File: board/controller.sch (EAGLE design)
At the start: 33 parts, among them J1 X_SIG, J10 COOLANT, J12 VIN, J13 GND, J15 A_SIG, J16 +5V, J17 PROBE, J18 FEED_OVERRIDE, J19 MOTOR_CURRENT, J2 Y_SIG, J20 WHEEL, J21 IR_RECEIVER, J22 DISPLAY, J23 ERROR, J24 HOLDING, J25 SPINDLE, J26 SD_READER, J3 Z_SIG, J4 RESET, J5 Z_DISPLAY, J6 FEED_HOLD, J8 CYCLE_START

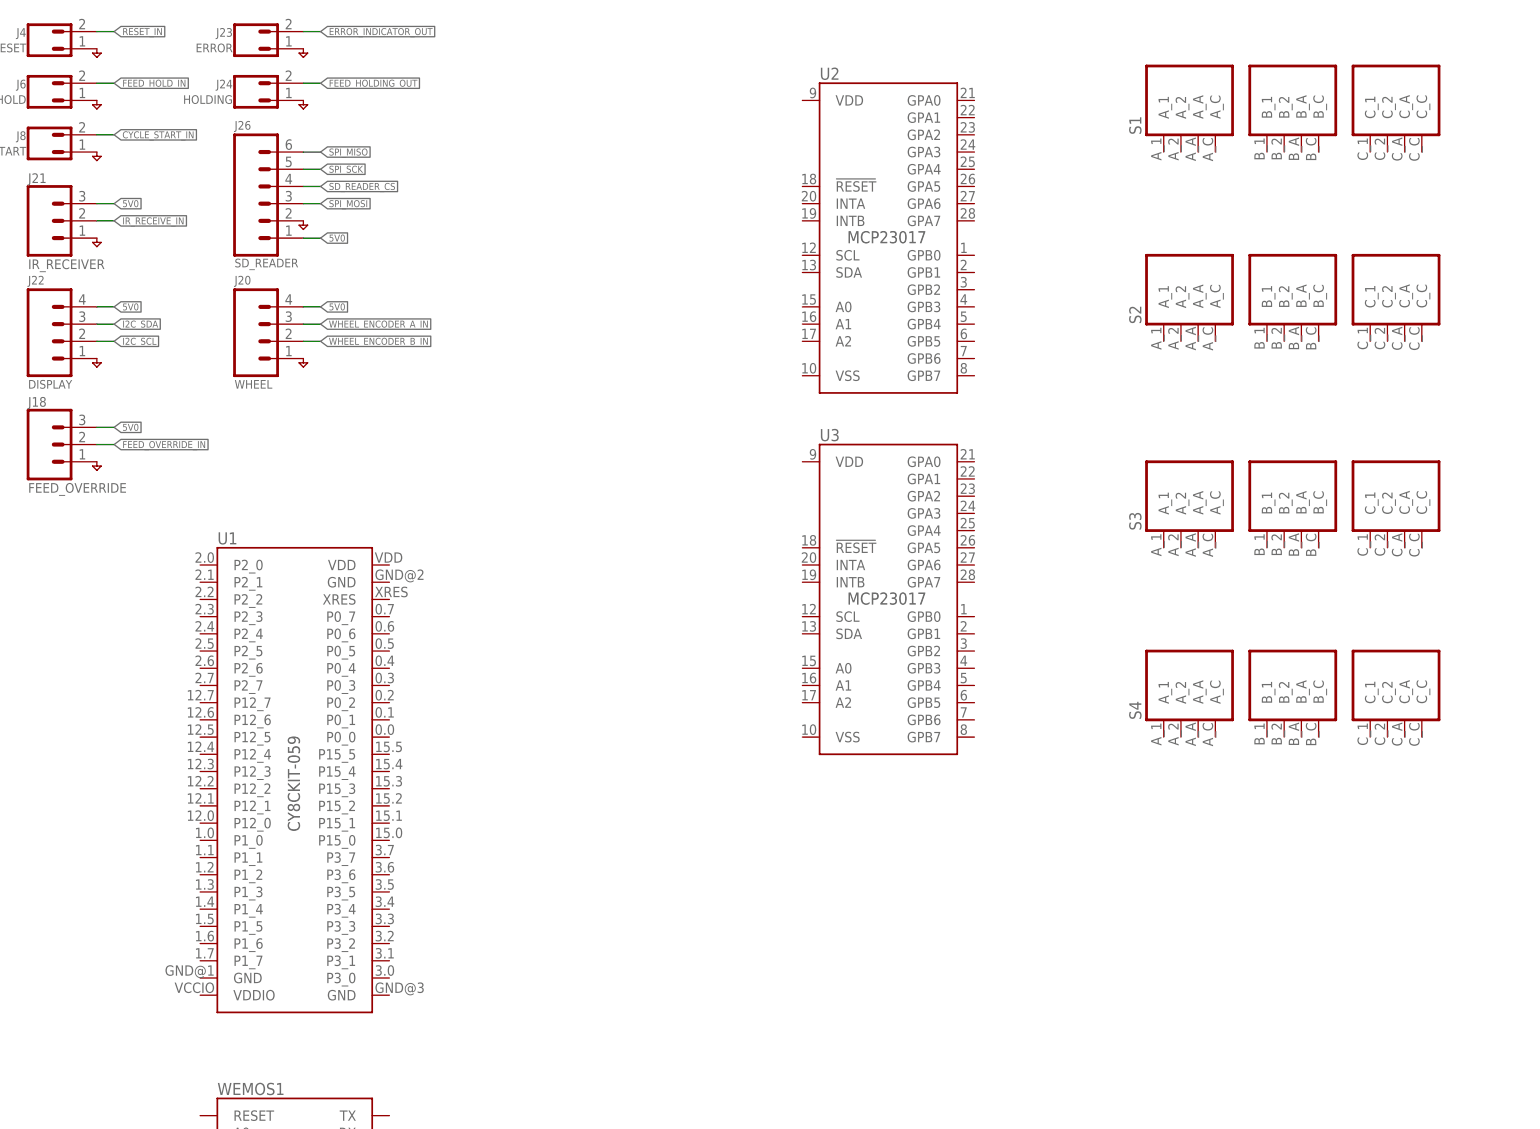
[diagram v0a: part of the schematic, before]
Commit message: started routing added datasheets
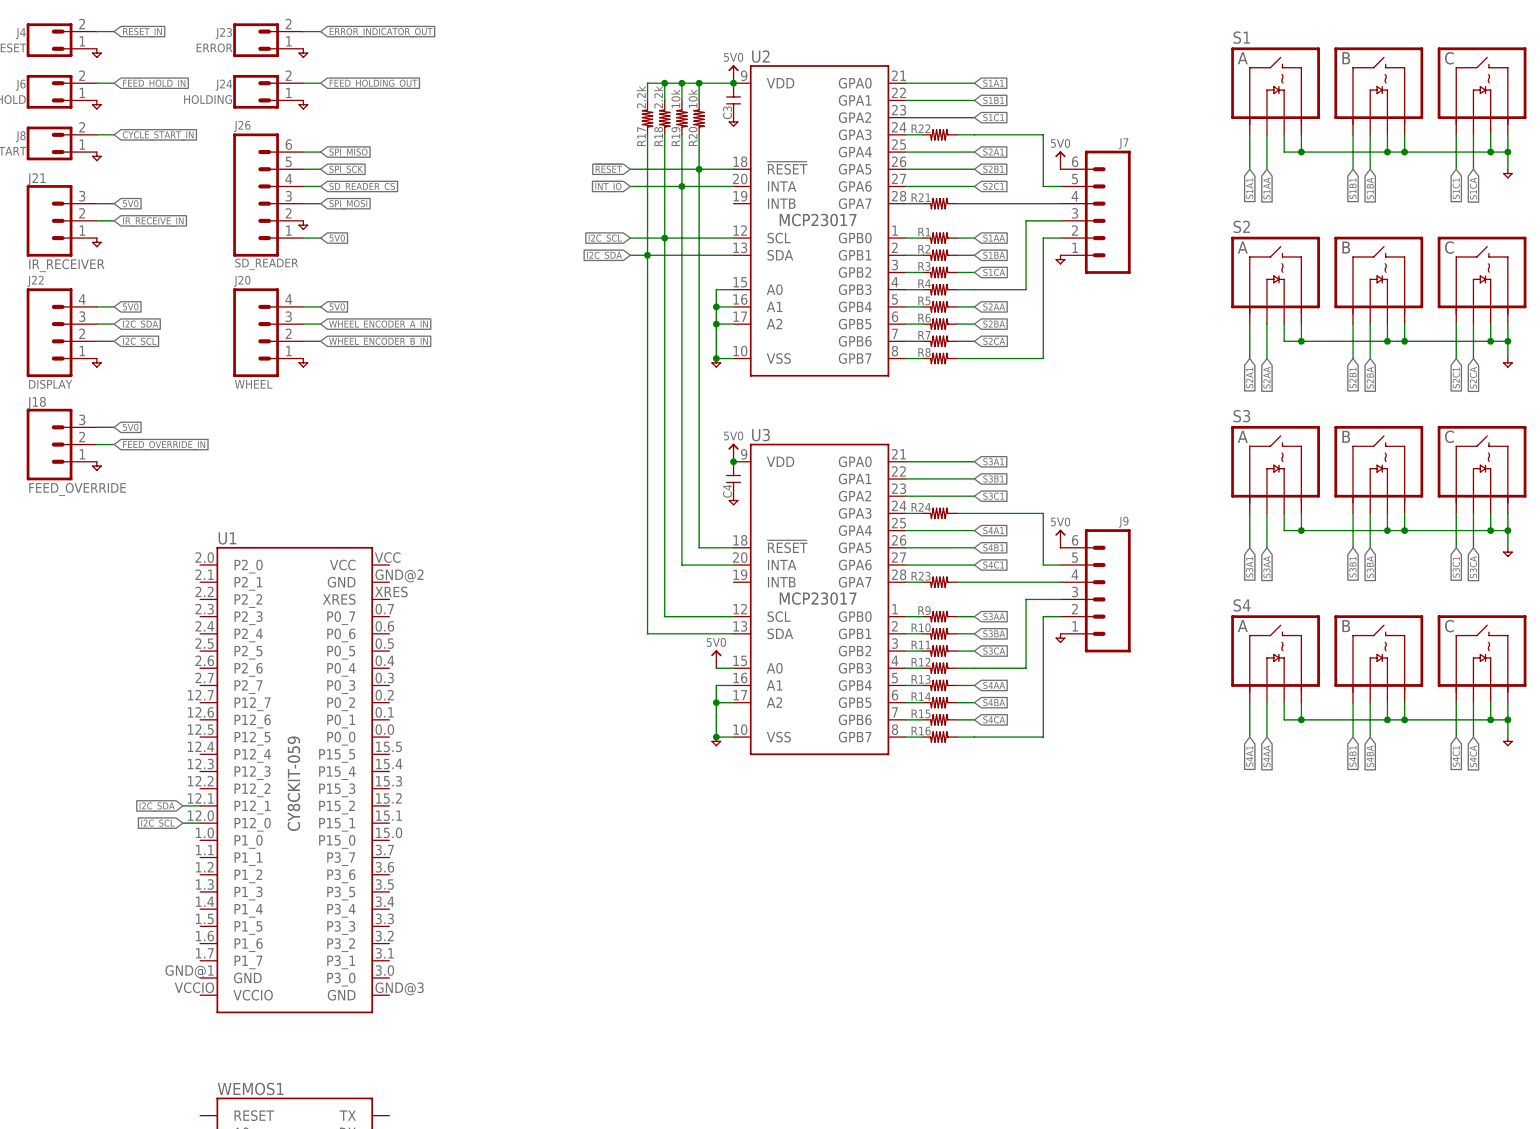
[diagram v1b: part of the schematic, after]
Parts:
- added C3, C4: (no value), holla:C-0603
- added J7, J9: (no value), holla:CONN-06-.100-VERT-HEADER
- added R1, R10, R11, R12, R13, R14, R15, R16, R2, R21, R22, R23, R24, R3, R4, R5, R6, R7, R8, R9: (no value), holla:R-0603
- added R17, R18: 2.2k, holla:R-0603
- added R19, R20: 10k, holla:R-0603
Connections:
- new net !INT_IO: R19.1, U2.INTA, U3.INTA
- new net !RESET: R20.1, U2.!RESET, U3.!RESET
- new net N$1: R1.1, U2.GPB0
- new net N$10: J9.5, R24.2
- new net N$11: J9.4, R23.2
- new net N$15: R3.1, U2.GPB2
- new net N$16: R4.1, U2.GPB3
- new net N$17: R5.1, U2.GPB4
- new net N$18: R6.1, U2.GPB5
- new net N$19: R7.1, U2.GPB6
- new net N$2: R2.1, U2.GPB1
- new net N$20: R8.1, U2.GPB7
- new net N$21: R9.1, U3.GPB0
- new net N$22: R10.1, U3.GPB1
- new net N$23: R11.1, U3.GPB2
- new net N$24: R12.1, U3.GPB3
- new net N$25: R13.1, U3.GPB4
- new net N$26: R14.1, U3.GPB5
- new net N$27: R15.1, U3.GPB6
- new net N$28: R16.1, U3.GPB7
- new net N$3: R22.1, U2.GPA3
- new net N$30: J7.2, R8.2
- new net N$4: J7.5, R22.2
- new net N$44: J9.3, R12.2
- new net N$48: J9.2, R16.2
- new net N$5: R21.1, U2.GPA7
- new net N$6: J7.3, R4.2
- new net N$7: J7.4, R21.2
- new net N$8: R24.1, U3.GPA3
- new net N$9: R23.1, U3.GPA7
- new net S1A1: S1.A_1, U2.GPA0
- new net S1AA: R1.2, S1.A_A
- new net S1B1: S1.B_1, U2.GPA1
- new net S1BA: R2.2, S1.B_A
- new net S1C1: S1.C_1, U2.GPA2
- new net S1CA: R3.2, S1.C_A
- new net S2A1: S2.A_1, U2.GPA4
- new net S2AA: R5.2, S2.A_A
- new net S2B1: S2.B_1, U2.GPA5
- new net S2BA: R6.2, S2.B_A
- new net S2C1: S2.C_1, U2.GPA6
- new net S2CA: R7.2, S2.C_A
- new net S3A1: S3.A_1, U3.GPA0
- new net S3AA: R9.2, S3.A_A
- new net S3B1: S3.B_1, U3.GPA1
- new net S3BA: R10.2, S3.B_A
- new net S3C1: S3.C_1, U3.GPA2
- new net S3CA: R11.2, S3.C_A
- new net S4A1: S4.A_1, U3.GPA4
- new net S4AA: R13.2, S4.A_A
- new net S4B1: S4.B_1, U3.GPA5
- new net S4BA: R14.2, S4.B_A
- new net S4C1: S4.C_1, U3.GPA6
- new net S4CA: R15.2, S4.C_A
- net 5V0: now also C3.1, C4.1, J7.6, J9.6, R17.2, R18.2, R19.2, R20.2, U2.VDD, U3.A0, U3.VDD
- net GND: now also C3.2, C4.2, J7.1, J9.1, S1.A_2, S1.A_C, S1.B_2, S1.B_C, S1.C_2, S1.C_C, S2.A_2, S2.A_C, S2.B_2, S2.B_C, S2.C_2, S2.C_C, S3.A_2, S3.A_C, S3.B_2, S3.B_C, S3.C_2, S3.C_C, S4.A_2, S4.A_C, S4.B_2, S4.B_C, S4.C_2, S4.C_C, U2.A0, U2.A1, U2.A2, U2.VSS, U3.A1, U3.A2, U3.VSS
- net I2C_SCL: now also R18.1, U1.P12_0, U2.SCL, U3.SCL
- net I2C_SDA: now also R17.1, U1.P12_1, U2.SDA, U3.SDA
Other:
- moved on the sheet: U2, U3

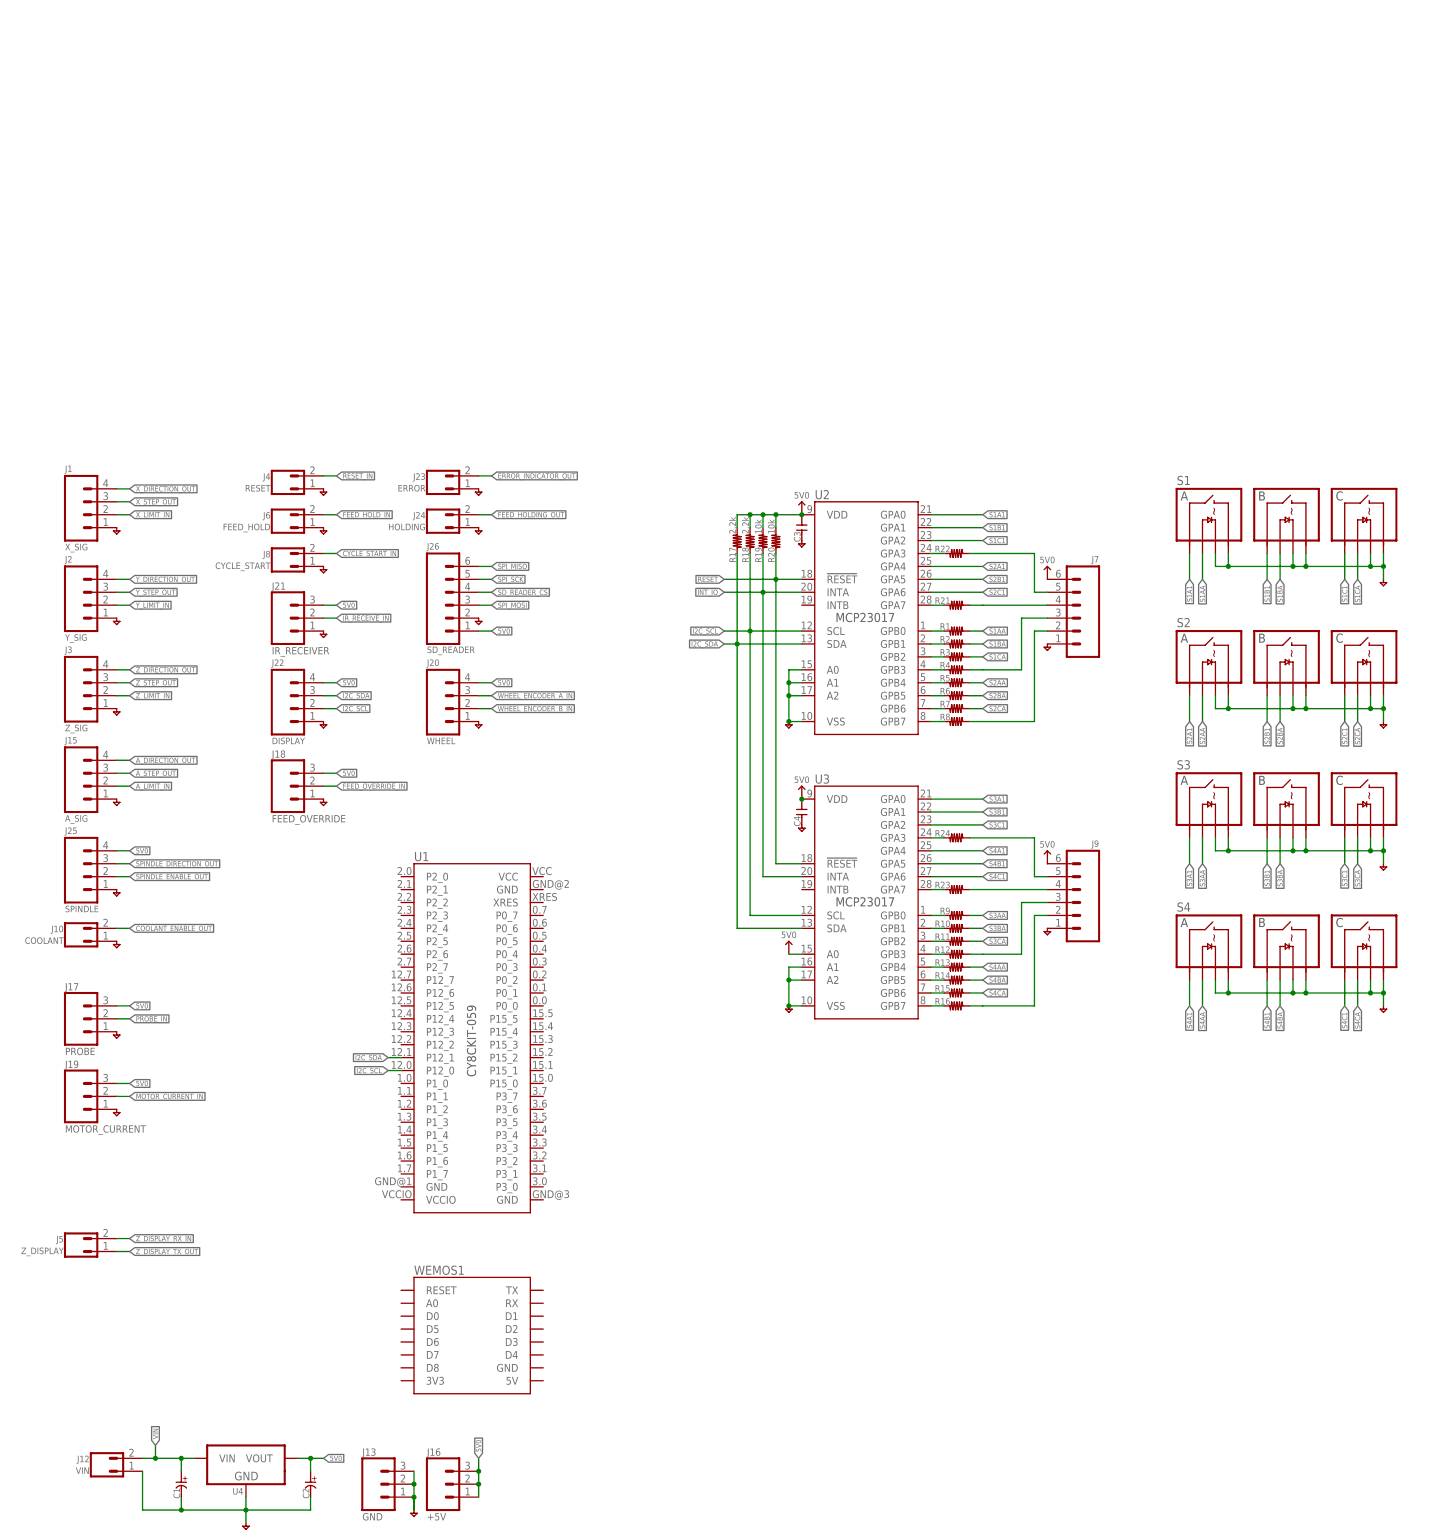
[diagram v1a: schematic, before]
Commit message: added datasheet continued routing
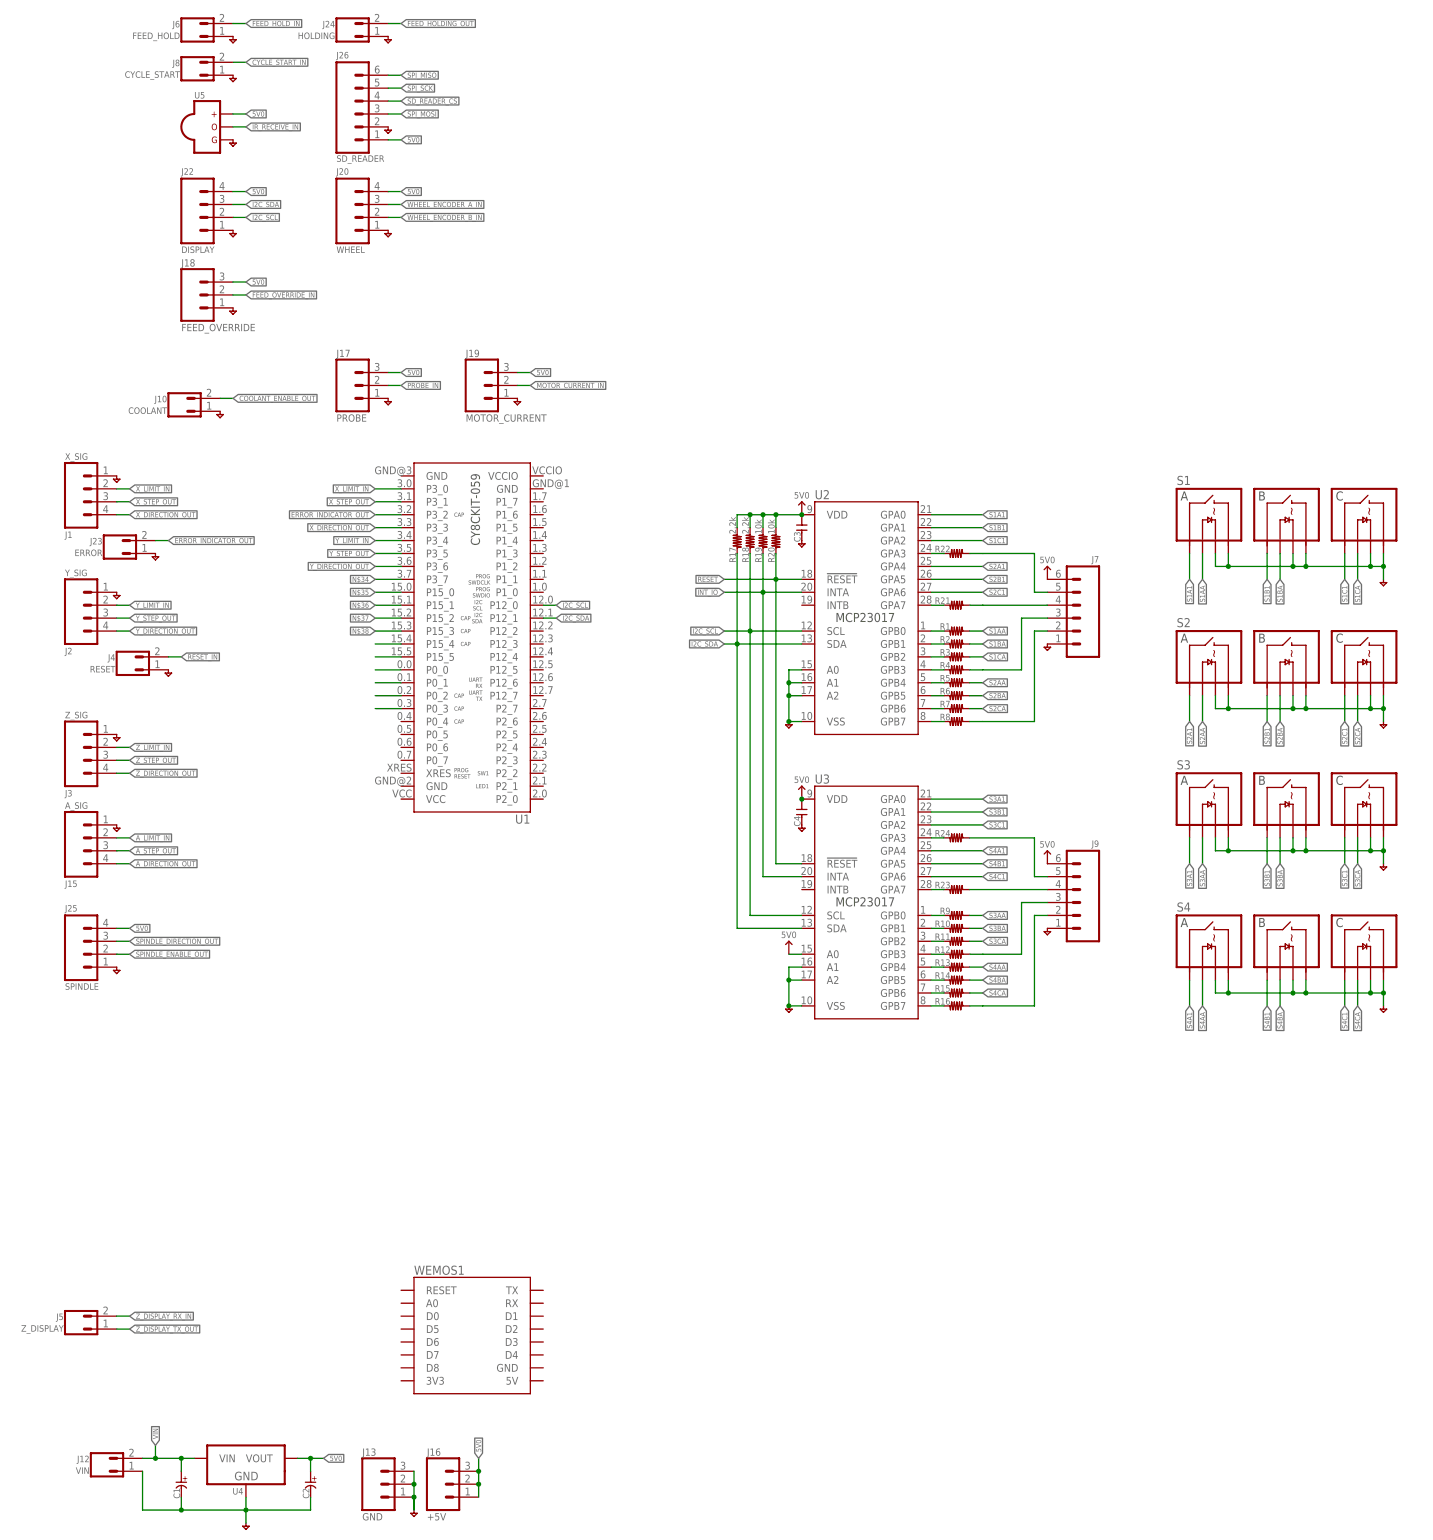
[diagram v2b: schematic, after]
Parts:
- removed J21: IR_RECEIVER, holla:CONN-03-.100
- added U5: SENSOR-IR-THRU, holla:SENSOR-IR-THRU
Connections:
- new net N$34: U1.P3_7
- new net N$35: U1.P15_0
- new net N$36: U1.P15_1
- new net N$37: U1.P15_2
- new net N$38: U1.P15_3
- new net N$39: U1.P15_4
- new net N$40: U1.P15_5
- new net N$41: U1.P0_0
- new net N$42: U1.P0_1
- new net N$43: U1.P0_2
- new net N$45: U1.P0_3
- net 5V0: now also U5.VCC; no longer J21.3
- net ERROR_INDICATOR_OUT: now also U1.P3_2
- net GND: now also U5.GND; no longer J21.1
- net IR_RECEIVE_IN: now also U5.VOUT; no longer J21.2
- net X_DIRECTION_OUT: now also U1.P3_3
- net X_LIMIT_IN: now also U1.P3_0
- net X_STEP_OUT: now also U1.P3_1
- net Y_DIRECTION_OUT: now also U1.P3_6
- net Y_LIMIT_IN: now also U1.P3_4
- net Y_STEP_OUT: now also U1.P3_5
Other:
- moved on the sheet: J1, J10, J15, J17, J18, J19, J2, J20, J22, J23, J24, J25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
